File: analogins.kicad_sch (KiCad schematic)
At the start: 13 parts, among them J19 Conn_01x04_Socket, U15 MCP6042

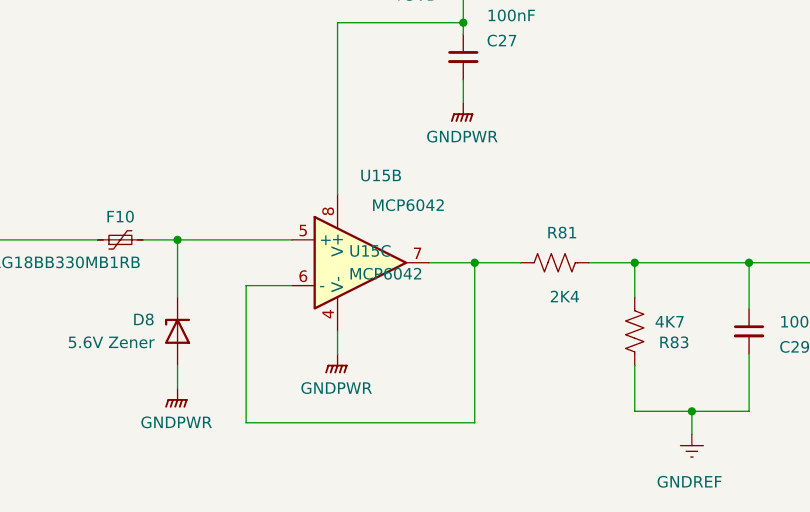
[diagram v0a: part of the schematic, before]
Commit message: Finalised Spindle DAC, working as expected
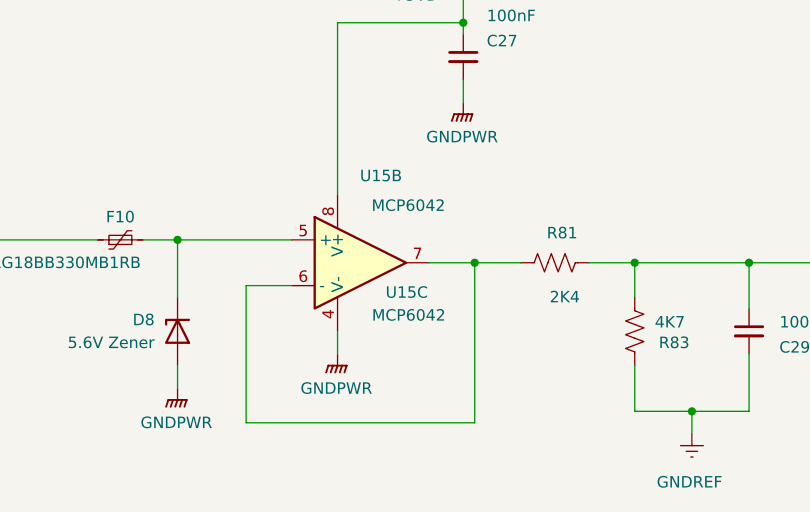
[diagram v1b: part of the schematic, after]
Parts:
- R80, R81: Digikey Part Number 311-4.70KFRCT-ND -> RMCF1206JT2K40CT-ND; Digikey URL https://www.digikey.com.au/en/products/detail/yageo/RC1206F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 -> https://www.digikey.com.au/en/products/detail/stackpole-ele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
- U15: Digikey URL 150-MCP6042T-E/MSVAOCT-ND -> https://www.digikey.com/en/products/detail/microchip-techno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
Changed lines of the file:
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@@
 			)
 		)
-		(property "Digikey Part Number" "311-4.70KFRCT-ND "
+		(property "Digikey Part Number" "RMCF1206JT2K40CT-ND"
 			(at 161.29 48.26 0)
 			(effects
@@
 			)
 		)
-		(property "Digikey URL" "https://www.digikey.com.au/en/products/detail/yageo/RC1206FR-074K7L/728887 "
+		(property "Digikey URL" "https://www.digikey.com.au/en/products/detail/stackpole-electronics-inc/RMCF1206JT2K40/1757490"
 			(at 161.29 48.26 0)
 			(effects
@@
 		(on_board yes)
 		(dnp no)
-		(fields_autoplaced yes)
 		(property "Reference" "U15"
-			(at 138.43 110.4899 0)
+			(at 142.494 115.062 0)
 			(effects
 				(font
@@
 		)
 		(property "Value" "MCP6042"
-			(at 138.43 113.0299 0)
+			(at 140.97 117.602 0)
 			(effects
 				(font
@@
 			)
 		)
-		(property "Digikey URL" "150-MCP6042T-E/MSVAOCT-ND"
+		(property "Digikey URL" "https://www.digikey.com/en/products/detail/microchip-technology/mcp6042t-e-snvao/9993094"
 			(at 139.7 111.76 0)
 			(effects
@@
 			)
 		)
-		(property "Digikey URL" "150-MCP6042T-E/MSVAOCT-ND"
+		(property "Digikey URL" "https://www.digikey.com/en/products/detail/microchip-technology/mcp6042t-e-snvao/9993094"
 			(at 139.7 111.76 0)
 			(effects
@@
 			)
 		)
-		(property "Digikey URL" "150-MCP6042T-E/MSVAOCT-ND"
+		(property "Digikey URL" "https://www.digikey.com/en/products/detail/microchip-technology/mcp6042t-e-snvao/9993094"
 			(at 139.7 48.26 0)
 			(effects
@@
 			)
 		)
-		(property "Digikey Part Number" "311-4.70KFRCT-ND "
+		(property "Digikey Part Number" "RMCF1206JT2K40CT-ND"
 			(at 161.29 111.76 0)
 			(effects
@@
 			)
 		)
-		(property "Digikey URL" "https://www.digikey.com.au/en/products/detail/yageo/RC1206FR-074K7L/728887 "
+		(property "Digikey URL" "https://www.digikey.com.au/en/products/detail/stackpole-electronics-inc/RMCF1206JT2K40/1757490"
 			(at 161.29 111.76 0)
 			(effects

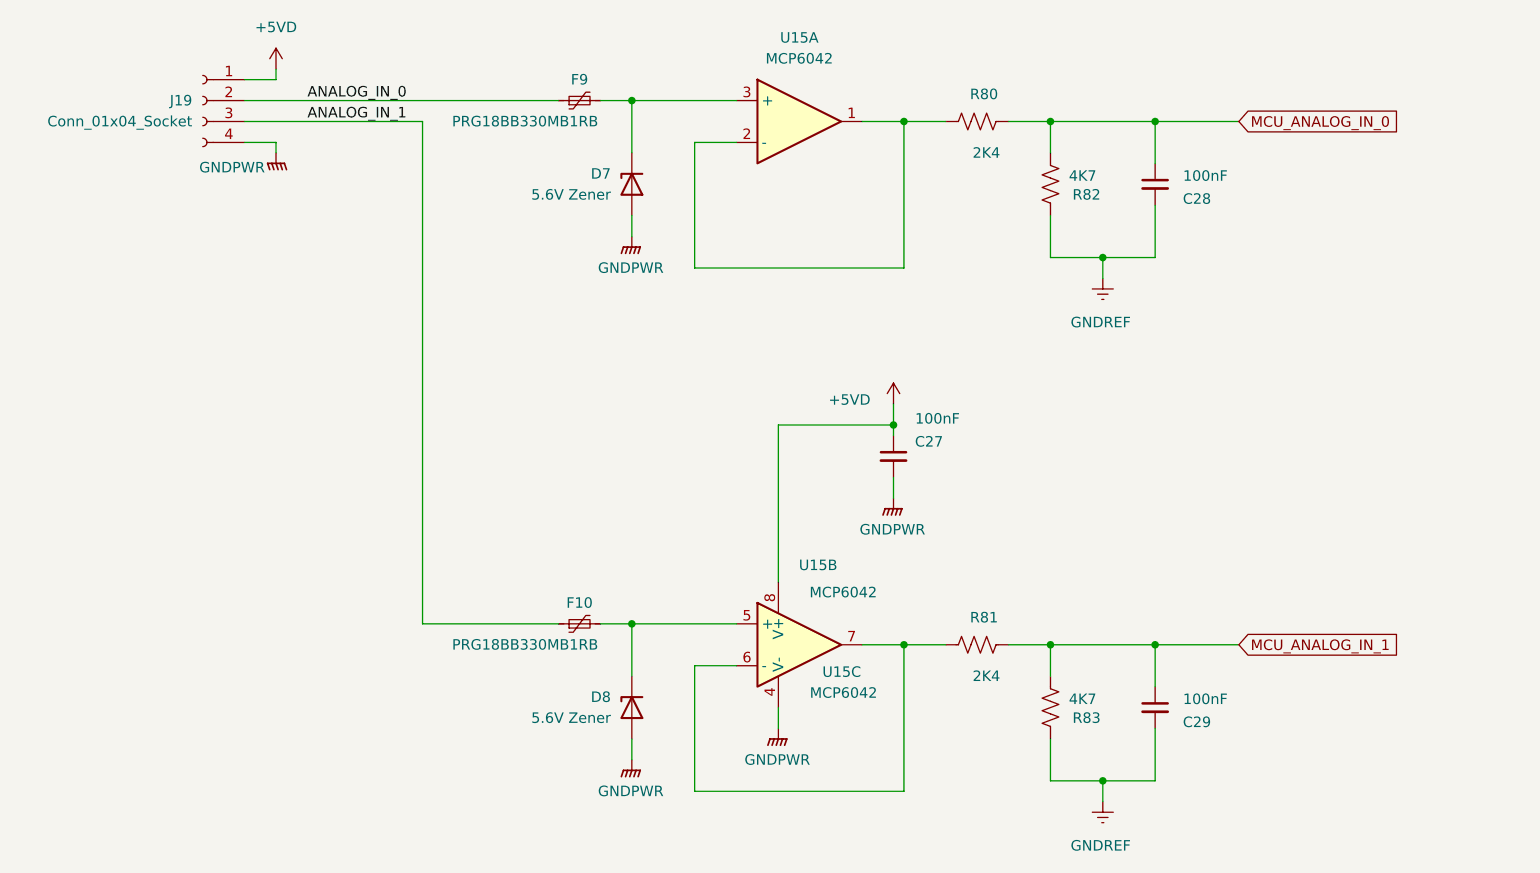
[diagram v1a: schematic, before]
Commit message: Switched terminal footprints over to a finer pitch. Corrected an issue with component reference values preventing proper use of multi channel rule areas. Component references for 4 channel optos are more straightforward as a result
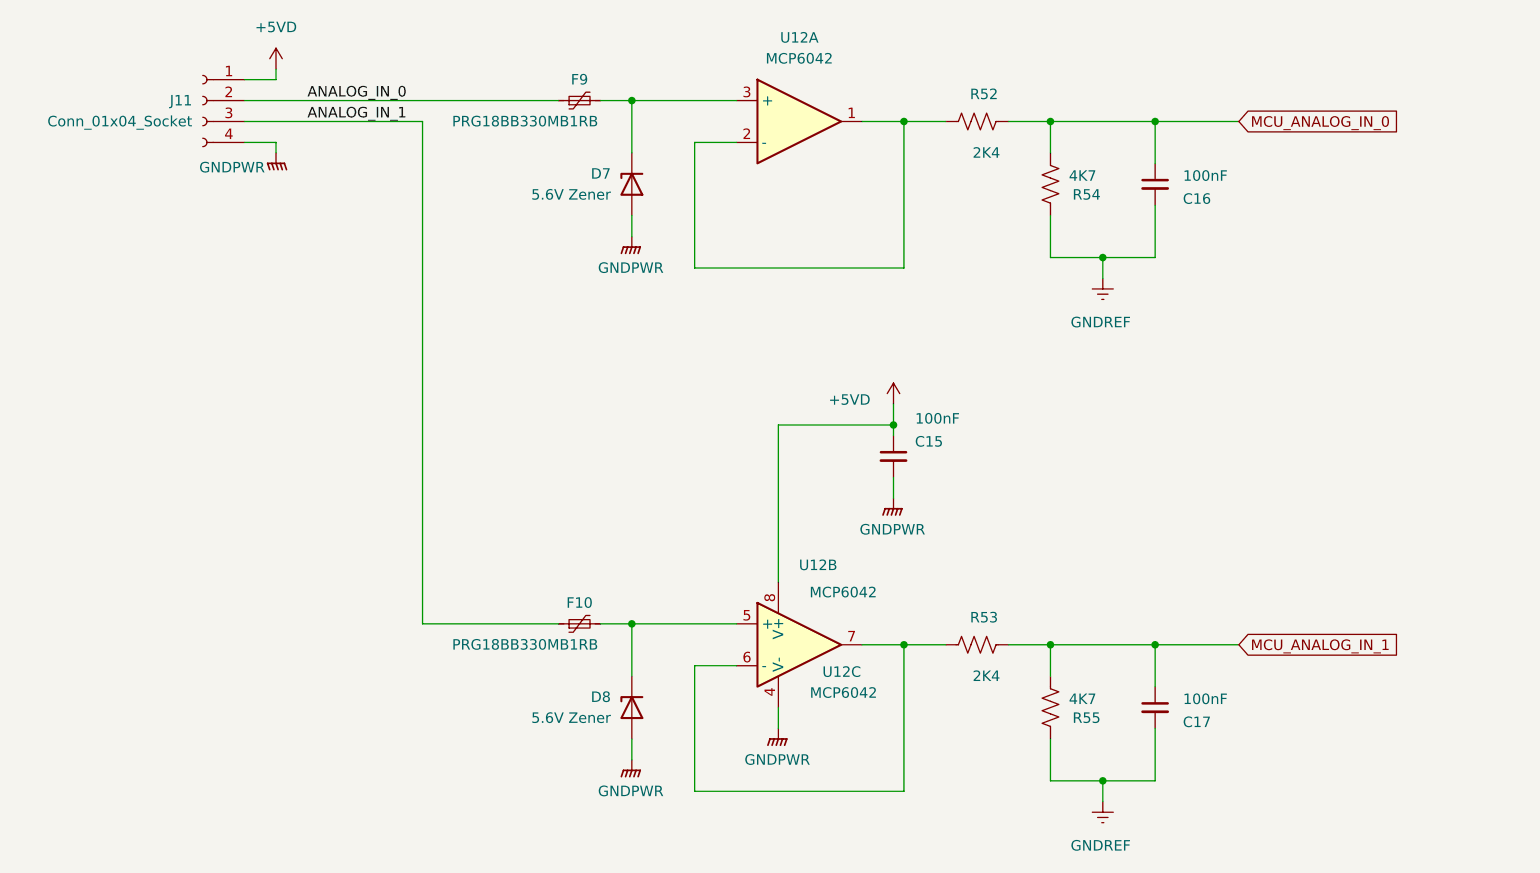
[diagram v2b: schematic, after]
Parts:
- J11: renamed from J19; footprint Amphenol QT:QT04ADP83V0000G -> 691412120004B:691412120004B; Digikey Part Number 1818-QT04ADP83V0000G-ND -> 732-691412120004B-ND; Digikey URL https://www.digikey.com.au/en/products/detail/amphenol-anyt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 -> https://www.digikey.com.au/en/products/detail/w%C3%BCrth-el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
- renumbered C27 to C15, C28 to C16, C29 to C17, R80 to R52, R81 to R53, R82 to R54, R83 to R55, U15 to U12
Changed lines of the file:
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@@
 		(on_board yes)
 		(dnp no)
-		(property "Reference" "#PWR0195"
+		(property "Reference" "#PWR0135"
 			(at 151.13 86.36 0)
 			(effects
@@
 			(project "Remora Nucleo F446ZE Hat"
 				(path "/5473abc6-7b93-43cc-a401-f691c4d7d7cf/c4dfed52-cba5-44a6-a641-6a90c0b6c0aa"
-					(reference "#PWR0195")
+					(reference "#PWR0135")
 					(unit 1)
 				)
@@
 		(on_board yes)
 		(dnp no)
-		(property "Reference" "R80"
+		(property "Reference" "R52"
 			(at 163.83 44.958 90)
 			(effects
@@
 			(project "Remora Nucleo F446ZE Hat"
 				(path "/5473abc6-7b93-43cc-a401-f691c4d7d7cf/c4dfed52-cba5-44a6-a641-6a90c0b6c0aa"
-					(reference "R80")
+					(reference "R52")
 					(unit 1)
 				)
@@
 		(on_board yes)
 		(dnp no)
-		(property "Reference" "U15"
+		(property "Reference" "U12"
 			(at 142.494 115.062 0)
 			(effects
@@
 			(project ""
 				(path "/5473abc6-7b93-43cc-a401-f691c4d7d7cf/c4dfed52-cba5-44a6-a641-6a90c0b6c0aa"
-					(reference "U15")
+					(reference "U12")
 					(unit 3)
 				)
@@
 		(on_board yes)
 		(dnp no)
-		(property "Reference" "C27"
+		(property "Reference" "C15"
 			(at 155.448 87.122 0)
 			(effects
@@
 			(project "Remora Nucleo F446ZE Hat"
 				(path "/5473abc6-7b93-43cc-a401-f691c4d7d7cf/c4dfed52-cba5-44a6-a641-6a90c0b6c0aa"
-					(reference "C27")
+					(reference "C15")
 					(unit 1)
 				)
@@
 		(on_board yes)
 		(dnp no)
-		(property "Reference" "R83"
+		(property "Reference" "R55"
 			(at 176.276 120.65 0)
 			(effects
@@
 			(project "Remora Nucleo F446ZE Hat"
 				(path "/5473abc6-7b93-43cc-a401-f691c4d7d7cf/c4dfed52-cba5-44a6-a641-6a90c0b6c0aa"
-					(reference "R83")
+					(reference "R55")
 					(unit 1)
 				)
@@
 		(dnp no)
 		(fields_autoplaced yes)
-		(property "Reference" "#PWR0192"
+		(property "Reference" "#PWR0132"
 			(at 119.38 67.31 0)
 			(effects
@@
 			(project "Remora Nucleo F446ZE Hat"
 				(path "/5473abc6-7b93-43cc-a401-f691c4d7d7cf/c4dfed52-cba5-44a6-a641-6a90c0b6c0aa"
-					(reference "#PWR0192")
+					(reference "#PWR0132")
 					(unit 1)
 				)
@@
 		(dnp no)
 		(fields_autoplaced yes)
-		(property "Reference" "#PWR0193"
+		(property "Reference" "#PWR0133"
 			(at 119.38 130.81 0)
 			(effects
@@
 			(project "Remora Nucleo F446ZE Hat"
 				(path "/5473abc6-7b93-43cc-a401-f691c4d7d7cf/c4dfed52-cba5-44a6-a641-6a90c0b6c0aa"
-					(reference "#PWR0193")
+					(reference "#PWR0133")
 					(unit 1)
 				)
@@
 		(dnp no)
 		(fields_autoplaced yes)
-		(property "Reference" "#PWR0194"
+		(property "Reference" "#PWR0134"
 			(at 137.16 127 0)
 			(effects
@@
 			(project "Remora Nucleo F446ZE Hat"
 				(path "/5473abc6-7b93-43cc-a401-f691c4d7d7cf/c4dfed52-cba5-44a6-a641-6a90c0b6c0aa"
-					(reference "#PWR0194")
+					(reference "#PWR0134")
 					(unit 1)
 				)
@@
 		(on_board yes)
 		(dnp no)
-		(property "Reference" "C28"
+		(property "Reference" "C16"
 			(at 187.96 57.658 0)
 			(effects
@@
 			(project "Remora Nucleo F446ZE Hat"
 				(path "/5473abc6-7b93-43cc-a401-f691c4d7d7cf/c4dfed52-cba5-44a6-a641-6a90c0b6c0aa"
-					(reference "C28")
+					(reference "C16")
 					(unit 1)
 				)
@@
 		(on_board yes)
 		(dnp no)
-		(property "Reference" "U15"
+		(property "Reference" "U12"
 			(at 141.986 102.108 0)
 			(effects
@@
 			(project ""
 				(path "/5473abc6-7b93-43cc-a401-f691c4d7d7cf/c4dfed52-cba5-44a6-a641-6a90c0b6c0aa"
-					(reference "U15")
+					(reference "U12")
 					(unit 2)
 				)
@@
 		(dnp no)
 		(fields_autoplaced yes)
-		(property "Reference" "J19"
+		(property "Reference" "J11"
 			(at 66.04 45.7199 0)
 			(effects
@@
 			)
 		)
-		(property "Footprint" "Amphenol QT:QT04ADP83V0000G"
+		(property "Footprint" "691412120004B:691412120004B"
 			(at 67.31 45.72 0)
 			(effects
@@
 			)
 		)
-		(property "Digikey Part Number" "1818-QT04ADP83V0000G-ND"
+		(property "Digikey Part Number" "732-691412120004B-ND"
 			(at 67.31 45.72 0)
 			(effects
@@
 			)
 		)
-		(property "Digikey URL" "https://www.digikey.com.au/en/products/detail/amphenol-anytek/QT04ADP83V0000G/25618782"
+		(property "Digikey URL" "https://www.digikey.com.au/en/products/detail/w%C3%BCrth-elektronik/691412120004B/11478393"
 			(at 67.31 45.72 0)
 			(effects
@@
 			(project "Remora Nucleo F446ZE Hat"
 				(path "/5473abc6-7b93-43cc-a401-f691c4d7d7cf/c4dfed52-cba5-44a6-a641-6a90c0b6c0aa"
-					(reference "J19")
+					(reference "J11")
 					(unit 1)
 				)
@@
 		(dnp no)
 		(fields_autoplaced yes)
-		(property "Reference" "U15"
+		(property "Reference" "U12"
 			(at 139.7 38.1 0)
 			(effects
@@
 			(project ""
 				(path "/5473abc6-7b93-43cc-a401-f691c4d7d7cf/c4dfed52-cba5-44a6-a641-6a90c0b6c0aa"
-					(reference "U15")
+					(reference "U12")
 					(unit 1)
 				)
@@
 		(on_board yes)
 		(dnp no)
-		(property "Reference" "C29"
+		(property "Reference" "C17"
 			(at 187.96 121.158 0)
 			(effects
@@
 			(project "Remora Nucleo F446ZE Hat"
 				(path "/5473abc6-7b93-43cc-a401-f691c4d7d7cf/c4dfed52-cba5-44a6-a641-6a90c0b6c0aa"
-					(reference "C29")
+					(reference "C17")
 					(unit 1)
 				)
@@
 		(on_board no)
 		(dnp no)
-		(property "Reference" "#PWR0198"
+		(property "Reference" "#PWR0138"
 			(at 176.53 137.16 0)
 			(effects
@@
 			(project "Remora Nucleo F446ZE Hat"
 				(path "/5473abc6-7b93-43cc-a401-f691c4d7d7cf/c4dfed52-cba5-44a6-a641-6a90c0b6c0aa"
-					(reference "#PWR0198")
+					(reference "#PWR0138")
 					(unit 1)
 				)
@@
 		(dnp no)
 		(fields_autoplaced yes)
-		(property "Reference" "#PWR0196"
+		(property "Reference" "#PWR0136"
 			(at 151.13 99.06 0)
 			(effects
@@
 			(project "Remora Nucleo F446ZE Hat"
 				(path "/5473abc6-7b93-43cc-a401-f691c4d7d7cf/c4dfed52-cba5-44a6-a641-6a90c0b6c0aa"
-					(reference "#PWR0196")
+					(reference "#PWR0136")
 					(unit 1)
 				)
@@
 		(on_board yes)
 		(dnp no)
-		(property "Reference" "R82"
+		(property "Reference" "R54"
 			(at 176.276 57.15 0)
 			(effects
@@
 			(project "Remora Nucleo F446ZE Hat"
 				(path "/5473abc6-7b93-43cc-a401-f691c4d7d7cf/c4dfed52-cba5-44a6-a641-6a90c0b6c0aa"
-					(reference "R82")
+					(reference "R54")
 					(unit 1)
 				)
@@
 		(dnp no)
 		(fields_autoplaced yes)
-		(property "Reference" "#PWR0190"
+		(property "Reference" "#PWR0130"
 			(at 76.2 45.72 0)
 			(effects
@@
 			(project "Remora Nucleo F446ZE Hat"
 				(path "/5473abc6-7b93-43cc-a401-f691c4d7d7cf/c4dfed52-cba5-44a6-a641-6a90c0b6c0aa"
-					(reference "#PWR0190")
+					(reference "#PWR0130")
 					(unit 1)
 				)
@@
 		(on_board no)
 		(dnp no)
-		(property "Reference" "#PWR0197"
+		(property "Reference" "#PWR0137"
 			(at 176.53 73.66 0)
 			(effects
@@
 			(project "Remora Nucleo F446ZE Hat"
 				(path "/5473abc6-7b93-43cc-a401-f691c4d7d7cf/c4dfed52-cba5-44a6-a641-6a90c0b6c0aa"
-					(reference "#PWR0197")
+					(reference "#PWR0137")
 					(unit 1)
 				)
@@
 		(on_board no)
 		(dnp no)
-		(property "Reference" "#PWR0191"
+		(property "Reference" "#PWR0131"
 			(at 76.2 57.15 0)
 			(effects
@@
 			(project "Remora Nucleo F446ZE Hat"
 				(path "/5473abc6-7b93-43cc-a401-f691c4d7d7cf/c4dfed52-cba5-44a6-a641-6a90c0b6c0aa"
-					(reference "#PWR0191")
+					(reference "#PWR0131")
 					(unit 1)
 				)
@@
 		(on_board yes)
 		(dnp no)
-		(property "Reference" "R81"
+		(property "Reference" "R53"
 			(at 163.83 108.458 90)
 			(effects
@@
 			(project "Remora Nucleo F446ZE Hat"
 				(path "/5473abc6-7b93-43cc-a401-f691c4d7d7cf/c4dfed52-cba5-44a6-a641-6a90c0b6c0aa"
-					(reference "R81")
-					(unit 1)
-				)
+					(reference "R53")
+					(unit 1)
+				)
